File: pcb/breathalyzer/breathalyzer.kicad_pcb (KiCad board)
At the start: 2 copper layers, 36.2 x 81.9 mm, 29 parts, among them J1 Conn_01x07_Pin, J2 MP-3B socket, Q1 Q_PMOS, Q2 NPN, SW1 PTS636SK43SMTR, SW2 SW_Push_Dual, U1 STM32F030K6Tx, U2 TLV73325PDBV, U4 TLV61070ADBV, U5 AY0438X-L

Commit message: pcb complete no errors
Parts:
- moved C1 1.01 mm to (137.8, 79.1), turned to -90 degrees
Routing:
- net GND: track 18.1 -> 53.7 mm, vias 2 -> 21
- net LCD_Clock: track 27.2 -> 20.0 mm
- net LCD_A1: track 54.1 -> 58.5 mm
- net USART1_RX: track 47.7 -> 52.0 mm
- net ADC_IN: track 89.8 -> 92.0 mm
- net LCD_B1: track 52.1 -> 54.0 mm
- net LCD_DATA: track 14.8 -> 16.1 mm
- net LCD_C1: track 23.7 -> 24.6 mm
- net LCD_D1: track 22.7 -> 23.6 mm
- net +2V5: track 123.8 -> 123.2 mm
- net Net-(BT1-+): track 8.38 -> 8.97 mm

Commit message: extra vias
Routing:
- net GND: vias 21 -> 27
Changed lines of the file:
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@@
 	)
 	(via
+		(at 131.445 99.695)
+		(size 0.6)
+		(drill 0.3)
+		(layers "F.Cu" "B.Cu")
+		(free yes)
+		(net 1)
+	)
+	(via
 		(at 143.51 98.6075)
 		(size 0.6)
@@
 	)
 	(via
+		(at 160.655 79.375)
+		(size 0.6)
+		(drill 0.3)
+		(layers "F.Cu" "B.Cu")
+		(free yes)
+		(net 1)
+	)
+	(via
 		(at 137.16 59.69)
 		(size 0.6)
@@
 	)
 	(via
+		(at 144.145 114.935)
+		(size 0.6)
+		(drill 0.3)
+		(layers "F.Cu" "B.Cu")
+		(free yes)
+		(net 1)
+	)
+	(via
 		(at 143.93881 94.496)
 		(size 0.6)
@@
 	)
 	(via
+		(at 133.35 114.935)
+		(size 0.6)
+		(drill 0.3)
+		(layers "F.Cu" "B.Cu")
+		(free yes)
+		(net 1)
+	)
+	(via
 		(at 131.445 86.36)
 		(size 0.6)
@@
 	)
 	(via
+		(at 158.75 41.91)
+		(size 0.6)
+		(drill 0.3)
+		(layers "F.Cu" "B.Cu")
+		(free yes)
+		(net 1)
+	)
+	(via
 		(at 131.445 58.42)
 		(size 0.6)
@@
 	)
 	(via
+		(at 154.305 78.105)
+		(size 0.6)
+		(drill 0.3)
+		(layers "F.Cu" "B.Cu")
+		(free yes)
+		(net 1)
+	)
+	(via
 		(at 150.495 91.44)
 		(size 0.6)
@@
 	)
 	(segment
-		(start 137.573334 77)
-		(end 140.205 77)
-		(width 0.6)
-		(layer "B.Cu")
-		(net 75)
-	)
-	(segment
-		(start 136.459 77.536)
-		(end 137.037334 77.536)
+		(start 149.225 86.35)
+		(end 145.5735 86.35)
 		(width 0.6)
 		(layer "B.Cu")
@@
 	)
 	(segment
-		(start 149.225 86.35)
-		(end 145.5735 86.35)
+		(start 139.7 86.073977)
+		(end 138.826785 85.200762)
 		(width 0.6)
 		(layer "B.Cu")
@@
 	)
 	(segment
-		(start 139.295999 86.176529)
-		(end 139.295999 85.669976)
+		(start 158.7835 50.161779)
+		(end 156.21 52.735279)
 		(width 0.6)
 		(layer "B.Cu")
@@
 	)
 	(segment
-		(start 158.7835 50.161779)
-		(end 156.21 52.735279)
+		(start 156.2435 64.198779)
+		(end 156.2435 81.9115)
 		(width 0.6)
 		(layer "B.Cu")
@@
 	)
 	(segment
-		(start 138.826785 85.200762)
-		(end 137.095566 85.200762)
+		(start 150.575481 40.035279)
+		(end 158.7835 48.243298)
 		(width 0.6)
 		(layer "B.Cu")
@@
 	)
 	(segment
-		(start 156.2435 64.198779)
-		(end 156.2435 81.9115)
+		(start 139.7 86.176529)
+		(end 139.7 86.073977)
 		(width 0.6)
 		(layer "B.Cu")
@@
 	)
 	(segment
-		(start 137.037334 77.536)
-		(end 137.573334 77)
+		(start 145.5735 86.35)
+		(end 145.415 86.1915)
 		(width 0.6)
 		(layer "B.Cu")
@@
 	)
 	(segment
-		(start 135.255 78.74)
-		(end 136.459 77.536)
+		(start 136.459 77.536)
+		(end 137.037334 77.536)
 		(width 0.6)
 		(layer "B.Cu")
@@
 	)
 	(segment
-		(start 150.575481 40.035279)
-		(end 158.7835 48.243298)
+		(start 137.573334 77)
+		(end 140.205 77)
 		(width 0.6)
 		(layer "B.Cu")
@@
 	)
 	(segment
-		(start 145.5735 86.35)
-		(end 145.415 86.1915)
+		(start 138.826785 85.200762)
+		(end 137.095566 85.200762)
 		(width 0.6)
 		(layer "B.Cu")
@@
 	)
 	(segment
-		(start 135.255 83.360196)
-		(end 135.255 78.74)
+		(start 156.21 64.165279)
+		(end 156.2435 64.198779)
 		(width 0.6)
 		(layer "B.Cu")
@@
 	)
 	(segment
-		(start 139.295999 85.669976)
-		(end 138.826785 85.200762)
+		(start 152.179 86.691)
+		(end 151.838 86.35)
 		(width 0.6)
 		(layer "B.Cu")
@@
 	)
 	(segment
-		(start 156.21 64.165279)
-		(end 156.2435 64.198779)
+		(start 156.2435 81.9115)
+		(end 153.75 84.405)
 		(width 0.6)
 		(layer "B.Cu")
@@
 	)
 	(segment
-		(start 139.7 86.176529)
-		(end 139.295999 86.176529)
+		(start 156.21 52.735279)
+		(end 156.21 64.165279)
 		(width 0.6)
 		(layer "B.Cu")
@@
 	)
 	(segment
-		(start 152.179 86.691)
-		(end 151.838 86.35)
+		(start 137.095566 85.200762)
+		(end 135.255 83.360196)
 		(width 0.6)
 		(layer "B.Cu")
@@
 	)
 	(segment
-		(start 156.2435 81.9115)
-		(end 153.75 84.405)
+		(start 137.037334 77.536)
+		(end 137.573334 77)
 		(width 0.6)
 		(layer "B.Cu")
@@
 	)
 	(segment
-		(start 156.21 52.735279)
-		(end 156.21 64.165279)
+		(start 151.838 86.35)
+		(end 149.225 86.35)
 		(width 0.6)
 		(layer "B.Cu")
@@
 	)
 	(segment
-		(start 151.838 86.35)
-		(end 149.225 86.35)
+		(start 158.7835 48.243298)
+		(end 158.7835 50.161779)
 		(width 0.6)
 		(layer "B.Cu")
@@
 	)
 	(segment
-		(start 158.7835 48.243298)
-		(end 158.7835 50.161779)
+		(start 135.255 78.74)
+		(end 136.459 77.536)
 		(width 0.6)
 		(layer "B.Cu")
@@
 	)
 	(segment
-		(start 137.095566 85.200762)
-		(end 135.255 83.360196)
+		(start 135.255 83.360196)
+		(end 135.255 78.74)
 		(width 0.6)
 		(layer "B.Cu")

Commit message: mounting holes
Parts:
- added H1: MountingHole, MountingHole:MountingHole_2.2mm_M2_ISO7380_Pad, F.Cu at (128.3, 40.6)
- added H1: MountingHole, MountingHole:MountingHole_2.2mm_M2_ISO7380_Pad, F.Cu at (159.4, 40.6)
- added H1: MountingHole, MountingHole:MountingHole_2.2mm_M2_ISO7380_Pad, F.Cu at (128.3, 90.2)
- BT1: value Battery -> 2x AA Battery
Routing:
- net LCD_A1: track 58.5 -> 60.4 mm
- net LCD_B1: track 54.0 -> 53.4 mm
- net GND: track 53.7 -> 53.8 mm, vias 27 -> 30

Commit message: no warnings
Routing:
- net LCD_A1: track 60.4 -> 58.6 mm
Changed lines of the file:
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@@
 		(tags "resistor")
 		(property "Reference" "R4"
-			(at 0 1.43 0)
+			(at 2.59 -0.01 0)
 			(layer "B.SilkS")
 			(effects
@@
 		(tags "capacitor")
 		(property "Reference" "C10"
-			(at 0 1.68 90)
+			(at 3.3125 0 90)
 			(layer "B.SilkS")
 			(effects
@@
 		(tags "resistor")
 		(property "Reference" "R5"
-			(at 0 1.43 180)
+			(at -0.237258 -1.26 180)
 			(layer "B.SilkS")
 			(effects
@@
 		(tags "Connector")
 		(property "Reference" "J1"
-			(at 0 0 0)
+			(at 0 -2.526 0)
 			(layer "B.SilkS")
 			(effects
@@
 		(tags "Potentiometer horizontal ACP CA9-H5")
 		(property "Reference" "RV1"
-			(at 0 3.65 180)
+			(at 0 3.245 180)
 			(layer "B.SilkS")
 			(effects
@@
 		(tags "SOT TO_SOT_SMD")
 		(property "Reference" "U4"
-			(at 0 2.4 90)
+			(at -1.76 2.86 90)
 			(layer "B.SilkS")
 			(effects
@@
 		(tags "capacitor")
 		(property "Reference" "C5"
-			(at 0 1.43 0)
+			(at 2.4 0.4525 0)
 			(layer "B.SilkS")
 			(effects
@@
 		(tags "capacitor")
 		(property "Reference" "C11"
-			(at 0 1.68 90)
+			(at -2.0875 1.68 90)
 			(layer "B.SilkS")
 			(effects
@@
 		(tags "Connector")
 		(property "Reference" "J2"
-			(at -3.75 0.525 180)
+			(at -3.75 1.874721 180)
 			(layer "B.SilkS")
 			(effects
@@
 		(tags "Connector")
 		(property "Reference" "BT1"
-			(at 0 0 90)
+			(at -0.0625 1.915 90)
 			(layer "B.SilkS")
 			(effects
@@
 		(tags "LQFP QFP")
 		(property "Reference" "U1"
-			(at 0 5.88 180)
+			(at 1.67 6.09 180)
 			(layer "B.SilkS")
 			(effects
@@
 		(tags "inductor")
 		(property "Reference" "L2"
-			(at 0 2.05 90)
+			(at -3.1875 0 90)
 			(layer "B.SilkS")
 			(effects
@@
 	)
 	(via
-		(at 131.445 58.42)
+		(at 132.08 58.42)
 		(size 0.6)
 		(drill 0.3)
@@
 	)
 	(segment
-		(start 131.4045 104.387417)
-		(end 131.588275 104.387417)
+		(start 128.905 101.887917)
+		(end 131.792083 104.775)
 		(width 0.4)
 		(layer "F.Cu")
@@
 	)
 	(segment
-		(start 132.662929 105.462071)
-		(end 133.3435 106.142641)
+		(start 128.905 99.8405)
+		(end 128.905 101.887917)
 		(width 0.4)
 		(layer "F.Cu")
@@
 	)
 	(segment
-		(start 140.9765 107.9295)
-		(end 142.24 106.666)
-		(width 0.4)
-		(layer "F.Cu")
-		(net 27)
-	)
-	(segment
-		(start 134.096641 107.9295)
-		(end 136.868636 107.9295)
+		(start 131.792083 104.775)
+		(end 132.08 104.775)
 		(width 0.4)
 		(layer "F.Cu")
@@
 	)
 	(segment
-		(start 132.603359 105.4025)
-		(end 132.662929 105.462071)
-		(width 0.4)
-		(layer "F.Cu")
-		(net 27)
-	)
-	(segment
-		(start 133.3435 106.142641)
-		(end 133.3435 107.176359)
+		(start 136.869636 107.9285)
+		(end 137.450364 107.9285)
 		(width 0.4)
 		(layer "F.Cu")
@@
 	)
 	(segment
-		(start 136.868636 107.9295)
-		(end 136.869636 107.9285)
+		(start 136.525 92.2205)
+		(end 128.905 99.8405)
 		(width 0.4)
 		(layer "F.Cu")
@@
 	)
 	(segment
-		(start 136.525 92.2205)
-		(end 128.905 99.8405)
+		(start 134.096641 107.9295)
+		(end 136.868636 107.9295)
 		(width 0.4)
 		(layer "F.Cu")
@@
 	)
 	(segment
-		(start 136.869636 107.9285)
-		(end 137.450364 107.9285)
+		(start 144.310003 81.905)
+		(end 144.752183 82.34718)
 		(width 0.4)
 		(layer "F.Cu")
@@
 	)
 	(segment
-		(start 144.310003 81.905)
-		(end 144.752183 82.34718)
+		(start 133.3435 106.0385)
+		(end 133.3435 107.176359)
 		(width 0.4)
 		(layer "F.Cu")
@@
 	)
 	(segment
-		(start 137.451364 107.9295)
-		(end 140.9765 107.9295)
+		(start 132.08 104.775)
+		(end 133.3435 106.0385)
 		(width 0.4)
 		(layer "F.Cu")
@@
 	)
 	(segment
-		(start 128.905 101.887917)
-		(end 131.4045 104.387417)
+		(start 137.450364 107.9285)
+		(end 137.451364 107.9295)
 		(width 0.4)
 		(layer "F.Cu")
@@
 	)
 	(segment
-		(start 128.905 99.8405)
-		(end 128.905 101.887917)
+		(start 136.868636 107.9295)
+		(end 136.869636 107.9285)
 		(width 0.4)
 		(layer "F.Cu")
@@
 	)
 	(segment
-		(start 131.588275 104.387417)
-		(end 132.662929 105.462071)
+		(start 140.9765 107.9295)
+		(end 142.24 106.666)
 		(width 0.4)
 		(layer "F.Cu")
@@
 	)
 	(segment
-		(start 137.450364 107.9285)
-		(end 137.451364 107.9295)
+		(start 137.451364 107.9295)
+		(end 140.9765 107.9295)
 		(width 0.4)
 		(layer "F.Cu")
@@
 	)
 	(segment
-		(start 144.630975 71.259025)
-		(end 144.630975 71.199525)
-		(width 0.4)
-		(layer "F.Cu")
-		(net 54)
-	)
-	(segment
 		(start 142.4825 48.682779)
 		(end 143.4435 47.721779)
@@
 	)
 	(segment
-		(start 143.929975 67.875304)
-		(end 144.007639 67.797639)
-		(width 0.4)
-		(layer "B.Cu")
-		(net 55)
-	)
-	(segment
 		(start 143.369975 68.435303)
 		(end 144.007639 67.797639)
@@
 	)
 	(segment
-		(start 128.8595 70.754897)
-		(end 128.8595 82.934384)
-		(width 0.4)
-		(layer "F.Cu")
-		(net 59)
-	)
-	(segment
-		(start 131.4605 90.8205)
-		(end 136.181364 90.8205)
-		(width 0.4)
-		(layer "F.Cu")
-		(net 59)
-	)
-	(segment
-		(start 130.81 56.505)
-		(end 130.81 58.063636)
-		(width 0.4)
-		(layer "F.Cu")
-		(net 59)
-	)
-	(segment
-		(start 130.81 68.804397)
+		(start 128.8595 82.934384)
 		(end 128.8595 70.754897)
 		(width 0.4)
@@
 	)
 	(segment
-		(start 136.181364 90.8205)
-		(end 137.795 92.434136)
-		(width 0.4)
-		(layer "F.Cu")
-		(net 59)
-	)
-	(segment
-		(start 128.92514 54.62014)
+		(start 130.81 52.735279)
 		(end 134.8625 48.682779)
 		(width 0.4)
@@
 	)
 	(segment
-		(start 130.81 84.455)
-		(end 130.81 90.17)
+		(start 134.8625 48.68278)
+		(end 134.8625 48.682779)
 		(width 0.4)
 		(layer "F.Cu")
@@
 	)
 	(segment
-		(start 138.505922 92.434136)
-		(end 140.335 90.605058)
+		(start 137.795 92.434136)
+		(end 136.181364 90.8205)
 		(width 0.4)
 		(layer "F.Cu")
@@
 	)
 	(segment
-		(start 130.744 58.710364)
-		(end 130.81 58.776364)
+		(start 131.4605 90.8205)
+		(end 130.81 90.17)
 		(width 0.4)
 		(layer "F.Cu")
@@
 	)
 	(segment
-		(start 130.81 90.17)
-		(end 131.4605 90.8205)
+		(start 138.505922 92.434136)
+		(end 137.795 92.434136)
 		(width 0.4)
 		(layer "F.Cu")
@@
 	)
 	(segment
-		(start 130.4895 84.1345)
-		(end 130.81 84.455)
+		(start 128.8595 70.754897)
+		(end 130.81 68.804397)
 		(width 0.4)
 		(layer "F.Cu")
@@
 	(segment
 		(start 140.335 90.605058)
-		(end 140.335 88.255)
-		(width 0.4)
-		(layer "F.Cu")
-		(net 59)
-	)
-	(segment
-		(start 130.744 58.129636)
-		(end 130.744 58.710364)
+		(end 138.505922 92.434136)
 		(width 0.4)
 		(layer "F.Cu")
@@
 	)
 	(segment
-		(start 130.81 58.776364)
-		(end 130.81 68.804397)
+		(start 130.059616 84.1345)
+		(end 128.8595 82.934384)
 		(width 0.4)
 		(layer "F.Cu")
@@
 	)
 	(segment
-		(start 128.8595 82.934384)
-		(end 130.059616 84.1345)
+		(start 130.81 90.17)
+		(end 130.81 84.455)
 		(width 0.4)
 		(layer "F.Cu")
@@
 	)
 	(segment
-		(start 137.795 92.434136)
-		(end 138.505922 92.434136)
+		(start 140.335 88.255)
+		(end 140.335 90.605058)
 		(width 0.4)
 		(layer "F.Cu")
@@
 	)
 	(segment
-		(start 128.92514 54.62014)
-		(end 130.81 56.505)
+		(start 130.81 84.455)
+		(end 130.4895 84.1345)
 		(width 0.4)
 		(layer "F.Cu")
@@
 	)
 	(segment
-		(start 128.8215 54.723779)
-		(end 128.92514 54.62014)
+		(start 130.4895 84.1345)
+		(end 130.059616 84.1345)
 		(width 0.4)
 		(layer "F.Cu")
@@
 	)
 	(segment
-		(start 130.059616 84.1345)
-		(end 130.4895 84.1345)
+		(start 136.181364 90.8205)
+		(end 131.4605 90.8205)
 		(width 0.4)
 		(layer "F.Cu")
@@
 	)
 	(segment
-		(start 130.81 58.063636)
-		(end 130.744 58.129636)
+		(start 130.81 68.804397)
+		(end 130.81 52.735279)
 		(width 0.4)
 		(layer "F.Cu")

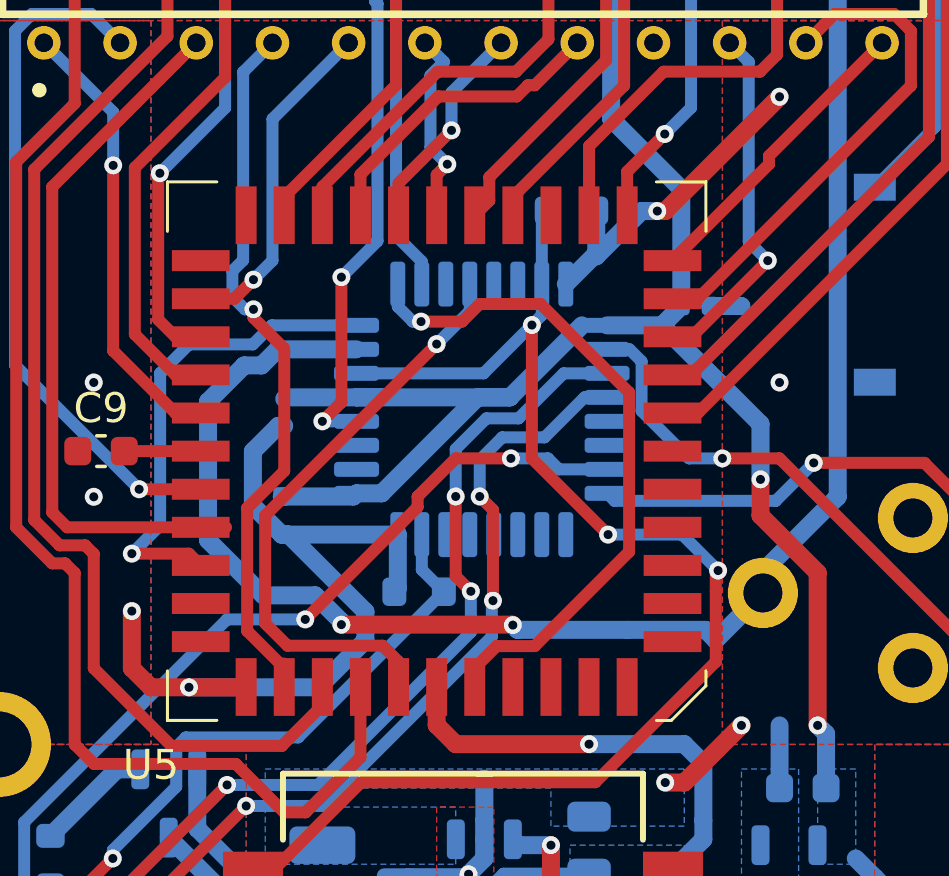
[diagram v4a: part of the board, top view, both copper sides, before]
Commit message: layout update
C closer to MCU
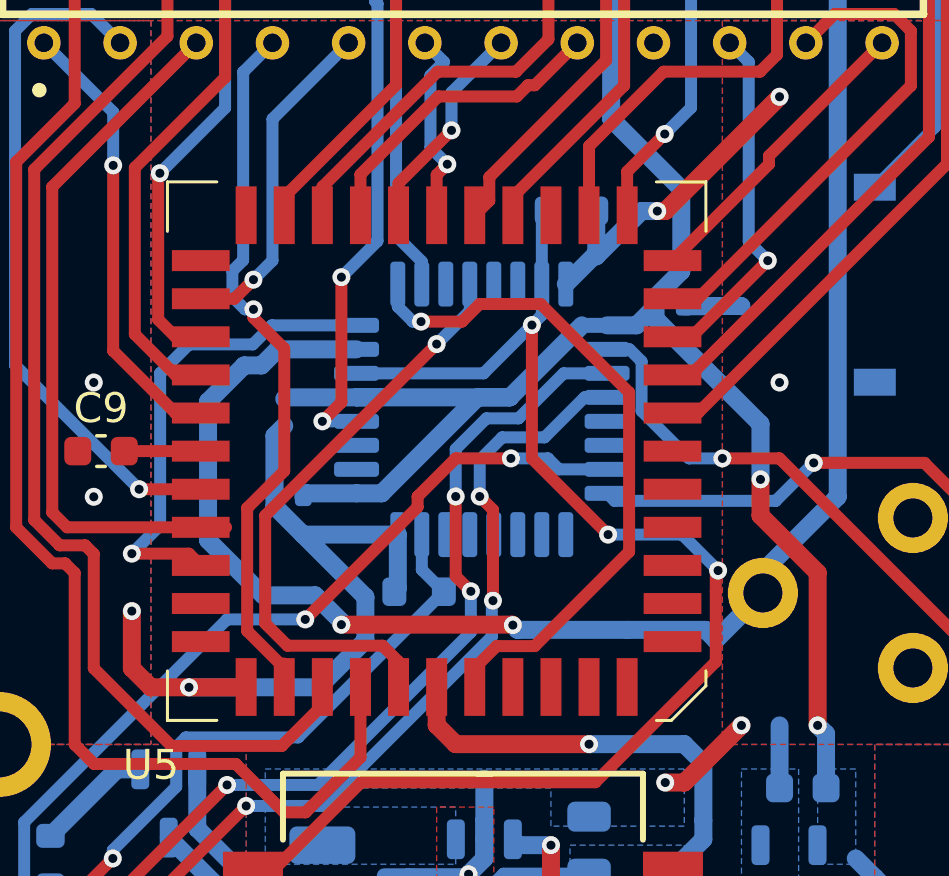
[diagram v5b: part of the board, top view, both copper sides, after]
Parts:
- moved C2 0.86 mm to (150.7, 75.6)
- moved C3 0.72 mm to (137.9, 81.9)
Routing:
- net GND: track 53.8 -> 53.1 mm
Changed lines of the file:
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@@
 	(footprint "Capacitor_SMD:C_0402_1005Metric"
 		(layer "B.Cu")
-		(at 137.23 81.905 180)
+		(at 137.95 81.915 180)
 		(descr "Capacitor SMD 0402 (1005 Metric), square (rectangular) end terminal, IPC-7351 nominal, (Body size source: IPC-SM-782 page 76, https://www.pcb-3d.com/wordpress/wp-content/uploads/ipc-sm-782a_amendment_1_and_2.pdf), generated with kicad-footprint-generator")
 		(tags "capacitor")
@@
 	(footprint "Capacitor_SMD:C_0402_1005Metric"
 		(layer "B.Cu")
-		(at 151.51 75.555)
+		(at 150.65 75.565)
 		(descr "Capacitor SMD 0402 (1005 Metric), square (rectangular) end terminal, IPC-7351 nominal, (Body size source: IPC-SM-782 page 76, https://www.pcb-3d.com/wordpress/wp-content/uploads/ipc-sm-782a_amendment_1_and_2.pdf), generated with kicad-footprint-generator")
 		(tags "capacitor")
@@
 	)
 	(segment
-		(start 136.75 81.905)
-		(end 136.75 80.395)
+		(start 137.47 81.915)
+		(end 137.47 79.876)
 		(width 0.6)
 		(layer "B.Cu")
@@
 	)
 	(segment
-		(start 137.710001 83.175)
-		(end 137.933808 83.175)
-		(width 0.6)
+		(start 141.9065 94.496)
+		(end 143.93881 94.496)
+		(width 0.4)
 		(layer "B.Cu")
 		(net 1)
 	)
 	(segment
-		(start 140.501 85.742192)
-		(end 140.501 86.702636)
+		(start 138.420001 83.175)
+		(end 137.47 82.224999)
 		(width 0.6)
 		(layer "B.Cu")
@@
 	)
 	(segment
-		(start 141.9065 94.496)
-		(end 143.93881 94.496)
-		(width 0.4)
-		(layer "B.Cu")
-		(net 1)
-	)
-	(segment
-		(start 138.938636 88.265)
-		(end 136.525 88.265)
+		(start 137.47 82.224999)
+		(end 137.47 81.915)
 		(width 0.6)
 		(layer "B.Cu")
@@
 	)
 	(segment
+		(start 140.501 85.255999)
+		(end 138.420001 83.175)
+		(width 0.6)
+		(layer "B.Cu")
+		(net 1)
+	)
+	(segment
 		(start 143.32 98.7975)
 		(end 143.51 98.6075)
@@
 	)
 	(segment
-		(start 144.465 92.69519)
-		(end 144.465 91.3075)
+		(start 138.938636 88.265)
+		(end 140.501 86.702636)
 		(width 0.6)
 		(layer "B.Cu")
@@
 	)
 	(segment
-		(start 136.75 80.395)
-		(end 137.594 79.551)
+		(start 134.62 88.265)
+		(end 138.938636 88.265)
+		(width 0.6)
+		(layer "B.Cu")
+		(net 1)
+	)
+	(segment
+		(start 144.465 92.69519)
+		(end 144.465 91.3075)
 		(width 0.6)
 		(layer "B.Cu")
@@
 	)
 	(segment
-		(start 144.465 93.3325)
-		(end 144.465 92.69519)
+		(start 141.58 83.175)
+		(end 138.420001 83.175)
 		(width 0.6)
 		(layer "B.Cu")
@@
 	)
 	(segment
-		(start 141.58 84.965)
-		(end 141.465 85.08)
+		(start 144.465 93.3325)
+		(end 144.465 92.69519)
 		(width 0.6)
 		(layer "B.Cu")
@@
 	)
 	(segment
-		(start 143.32 99.8775)
-		(end 143.32 98.7975)
+		(start 141.58 84.965)
+		(end 141.465 85.08)
 		(width 0.6)
 		(layer "B.Cu")
@@
 	)
 	(segment
-		(start 136.75 82.214999)
-		(end 136.75 81.905)
+		(start 151.98 75.565)
+		(end 151.99 75.555)
 		(width 0.6)
 		(layer "B.Cu")
@@
 	)
 	(segment
-		(start 137.710001 83.175)
-		(end 136.75 82.214999)
+		(start 143.32 99.8775)
+		(end 143.32 98.7975)
 		(width 0.6)
 		(layer "B.Cu")
@@
 	)
 	(segment
-		(start 136.525 88.265)
-		(end 134.62 88.265)
+		(start 148.195 73.9)
+		(end 149.705 72.39)
 		(width 0.6)
 		(layer "B.Cu")
@@
 	)
 	(segment
-		(start 148.195 73.9)
-		(end 149.705 72.39)
+		(start 140.501 86.702636)
+		(end 140.501 85.255999)
 		(width 0.6)
 		(layer "B.Cu")
@@
 	)
 	(segment
-		(start 137.933808 83.175)
-		(end 140.501 85.742192)
+		(start 151.13 75.565)
+		(end 151.98 75.565)
 		(width 0.6)
 		(layer "B.Cu")
@@
 	)
 	(segment
-		(start 140.501 86.702636)
-		(end 138.938636 88.265)
-		(width 0.6)
-		(layer "B.Cu")
-		(net 1)
-	)
-	(segment
-		(start 141.58 83.175)
-		(end 137.710001 83.175)
+		(start 148.195 73.81)
+		(end 148.195 73.9)
 		(width 0.6)
 		(layer "B.Cu")
@@
 	)
 	(segment
-		(start 137.594 79.551)
+		(start 137.47 79.876)
 		(end 137.795 79.551)
 		(width 0.6)
@@
 	)
 	(segment
-		(start 148.195 73.81)
-		(end 148.195 73.9)
-		(width 0.6)
-		(layer "B.Cu")
-		(net 1)
-	)
-	(segment
 		(start 146.05 100.5125)
 		(end 146.685 99.8775)
@@
 	)
 	(segment
+		(start 140.205 81.8)
+		(end 138.545 81.8)
+		(width 0.6)
+		(layer "B.Cu")
+		(net 3)
+	)
+	(segment
 		(start 148.690906 69.315906)
 		(end 151.03 71.655)
@@
 	)
 	(segment
-		(start 150.385 76.2)
-		(end 151.03 75.555)
+		(start 150.17 75.255)
+		(end 151.03 74.395)
 		(width 0.6)
 		(layer "B.Cu")
@@
 	)
 	(segment
-		(start 137.71 81.905)
-		(end 140.1 81.905)
-		(width 0.6)
-		(layer "B.Cu")
-		(net 3)
-	)
-	(segment
-		(start 159.621 95.24)
-		(end 158.115 95.24)
+		(start 151.03 74.395)
+		(end 151.03 71.655)
 		(width 0.6)
 		(layer "B.Cu")
@@
 	)
 	(segment
-		(start 158.115 95.24)
-		(end 157.48 94.605)
+		(start 149.535 76.2)
+		(end 150.17 75.565)
 		(width 0.6)
 		(layer "B.Cu")
@@
 	)
 	(segment
-		(start 140.1 81.905)
-		(end 140.205 81.8)
+		(start 159.621 95.24)
+		(end 158.115 95.24)
 		(width 0.6)
 		(layer "B.Cu")
@@
 	)
 	(segment
-		(start 150.385 76.2)
-		(end 148.555 76.2)
+		(start 158.115 95.24)
+		(end 157.48 94.605)
 		(width 0.6)
 		(layer "B.Cu")
@@
 	)
 	(segment
-		(start 153.67 79.485)
-		(end 150.385 76.2)
-		(width 0.6)
-		(layer "B.Cu")
-		(net 3)
-	)
-	(segment
 		(start 145.316238 78.6)
 		(end 147.716238 76.2)
@@
 	)
 	(segment
+		(start 153.67 79.485)
+		(end 150.17 75.985)
+		(width 0.6)
+		(layer "B.Cu")
+		(net 3)
+	)
+	(segment
 		(start 148.690906 42.796185)
 		(end 148.690906 69.315906)
@@
 	)
 	(segment
+		(start 148.555 76.2)
+		(end 149.535 76.2)
+		(width 0.6)
+		(layer "B.Cu")
+		(net 3)
+	)
+	(segment
 		(start 141.043762 81.8)
 		(end 144.243762 78.6)
@@
 	)
 	(segment
-		(start 151.03 71.655)
-		(end 151.03 75.555)
+		(start 150.17 75.565)
+		(end 150.17 75.255)
 		(width 0.6)
 		(layer "B.Cu")
@@
 	)
 	(segment
+		(start 150.17 75.985)
+		(end 150.17 75.565)
+		(width 0.6)
+		(layer "B.Cu")
+		(net 3)
+	)
+	(segment
 		(start 140.205 78.6)
 		(end 145.316238 78.6)
 		(width 0.6)
 		(layer "B.Cu")
+		(net 3)
+	)
+	(segment
+		(start 138.545 81.8)
+		(end 138.43 81.915)
+		(width 0.6)
+		(layer "B.Cu")

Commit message: adjustments
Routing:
- net GND: track 53.1 -> 52.0 mm
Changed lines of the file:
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@@
-	)
-	(segment
-		(start 130.0025 94.8675)
-		(end 131.105 94.8675)
-		(width 0.6)
-		(layer "B.Cu")
-		(net 1)
 	)
 	(segment
